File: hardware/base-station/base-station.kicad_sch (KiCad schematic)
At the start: 11 parts, among them J1 USB_C_Receptacle_USB2.0_16P, Q1 AO3400A, U2 TPB4056A20

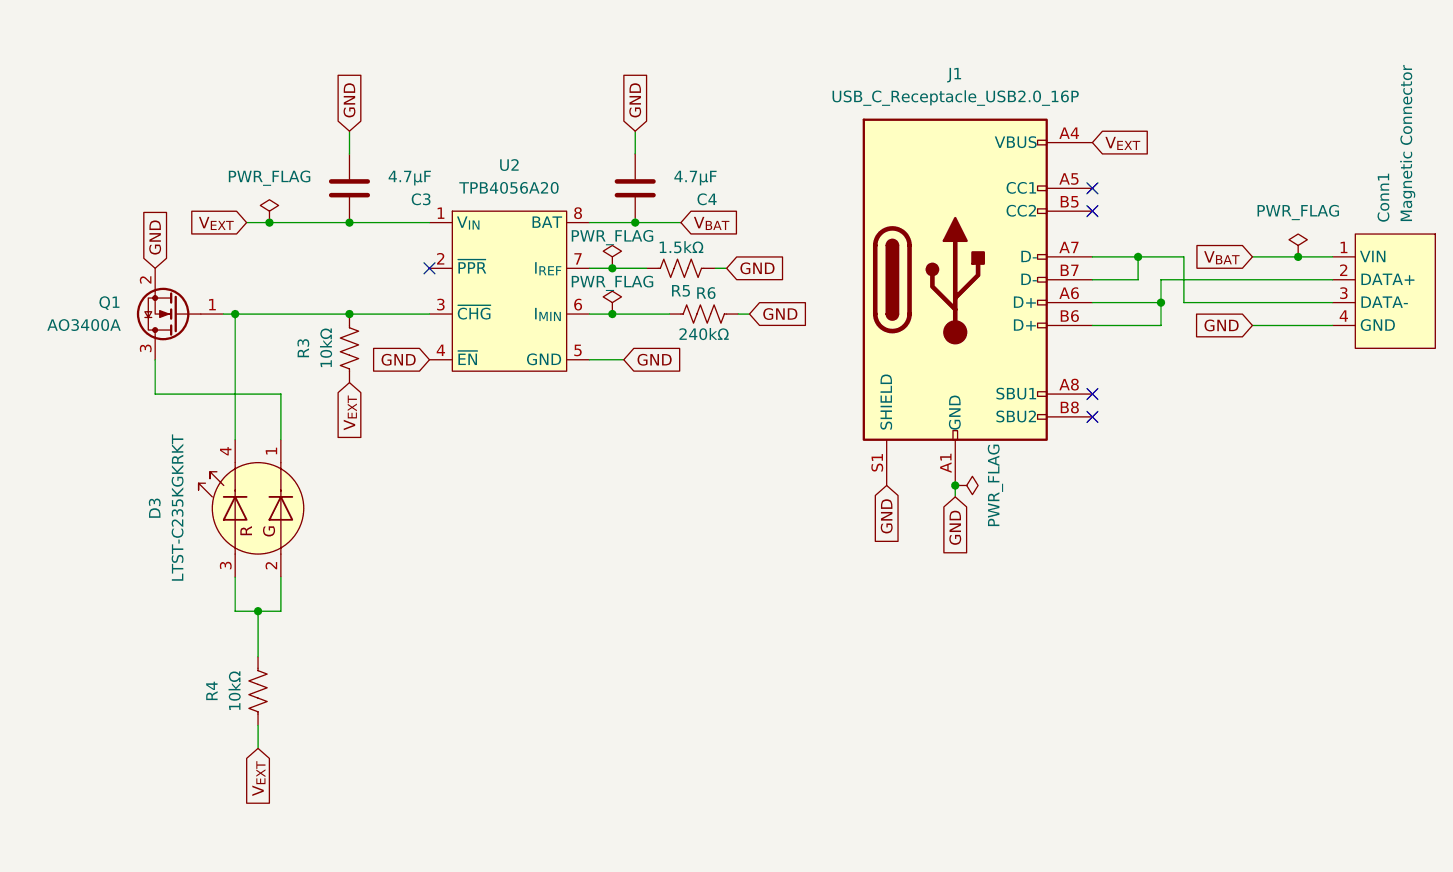
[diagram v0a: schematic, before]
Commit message: Add schematic review checklist for Plantie hardware and revert charging IC to MCP73831T
This commit introduces a comprehensive checklist for the electrical review of the control unit and base station schematics. The checklist includes must-fix items, placeholders for final values, design intent confirmations, minor notes, and verified components. It aims to ensure all critical aspects are addressed before fabrication.
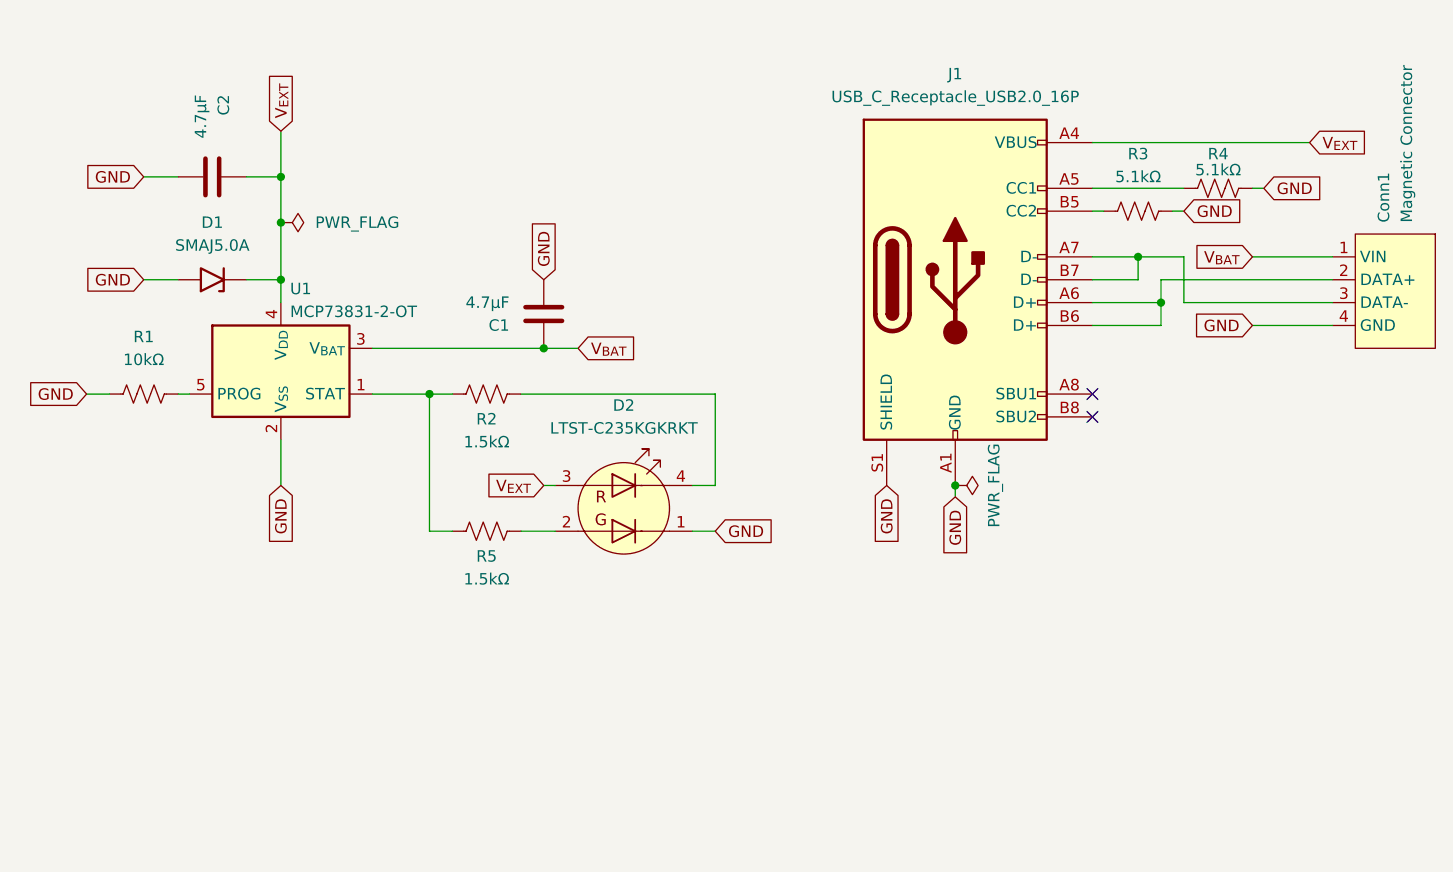
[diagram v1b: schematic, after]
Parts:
- removed C3, C4: 4.7μF, Capacitor_SMD:C_0402_1005Metric, symbol Device:C
- removed D3: LTST-C235KGKRKT, LED_SMD:LED_LiteOn_LTST-C235KGKRKT, symbol LED:LTST-C235KGKRKT
- removed Q1: AO3400A, Package_TO_SOT_SMD:SOT-23, symbol Transistor_FET:AO3400A
- removed R6: 240kΩ, Resistor_SMD:R_0805_2012Metric_Pad1.20x1.40mm_HandSolder, symbol Device:R_US
- removed U2: TPB4056A20, Package_SO:SOP-8-1EP_4.57x4.57mm_P1.27mm_EP4.57x4.45mm_ThermalVias, symbol Custom_Symbols:TPB4056A20
- added C1, C2: 4.7μF, Capacitor_SMD:C_0402_1005Metric, symbol Device:C
- added D1: SMAJ5.0A, Diode_SMD:D_SMA, symbol Diode:SMAJ5.0A
- added D2: LTST-C235KGKRKT, LED_SMD:LED_LiteOn_LTST-C235KGKRKT, symbol LED:LTST-C235KGKRKT
- added R1: 10kΩ, symbol Device:R_US
- added R2: 1.5kΩ, symbol Device:R_US
- added U1: MCP73831-2-OT, Package_TO_SOT_SMD:SOT-23-5, symbol Battery_Management:MCP73831-2-OT
- R3, R4: value 10kΩ -> 5.1kΩ; footprint Resistor_SMD:R_0805_2012Metric_Pad1.20x1.40mm_HandSolder -> (none)
- R5: footprint Resistor_SMD:R_0805_2012Metric_Pad1.20x1.40mm_HandSolder -> (none)
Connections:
- net GND: now also R3.2, R4.2, C1.2, C2.2, D1.2 (A2), D2.1 (K2), R1.1, U1.2 (V_{SS}); no longer R5.1
- net V_{BAT}: now also C1.1, U1.3 (V_{BAT})
- net V_{EXT}: now also C2.1, D1.1 (A1), D2.3 (A1), U1.4 (V_{DD}); no longer R3.1, R4.1
- net at R5.2: now also D2.2 (A2)
- net at J1.A5 (CC1): now also R4.1
- net at J1.B5 (CC2): now also R3.1
- new net: R2.1, R5.1, U1.1 (STAT)
- new net: R1.2, U1.5 (PROG)
- new net: D2.4 (K1), R2.2
- no-connect marks 5 -> 2
